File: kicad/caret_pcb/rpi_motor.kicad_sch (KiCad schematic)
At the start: 6 parts, among them J12 X+, J13 Y+, J14 Raspberry_Pi_2_3, J15 PWR IN

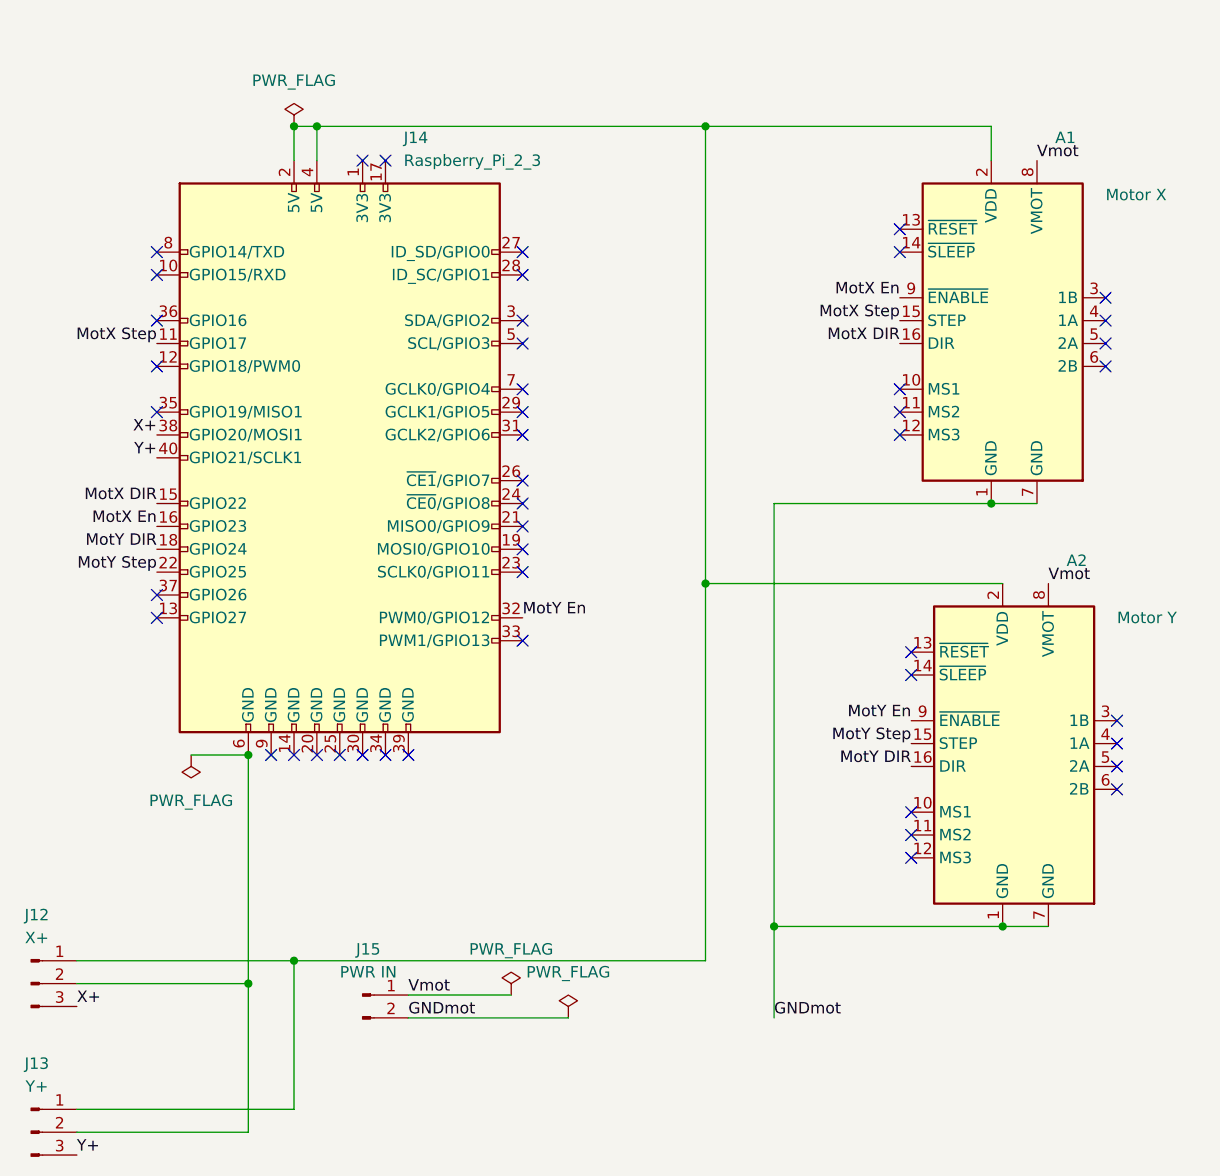
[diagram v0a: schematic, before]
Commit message: caret_pcb: fix piezo sensor power line, fix rpi shield schematic
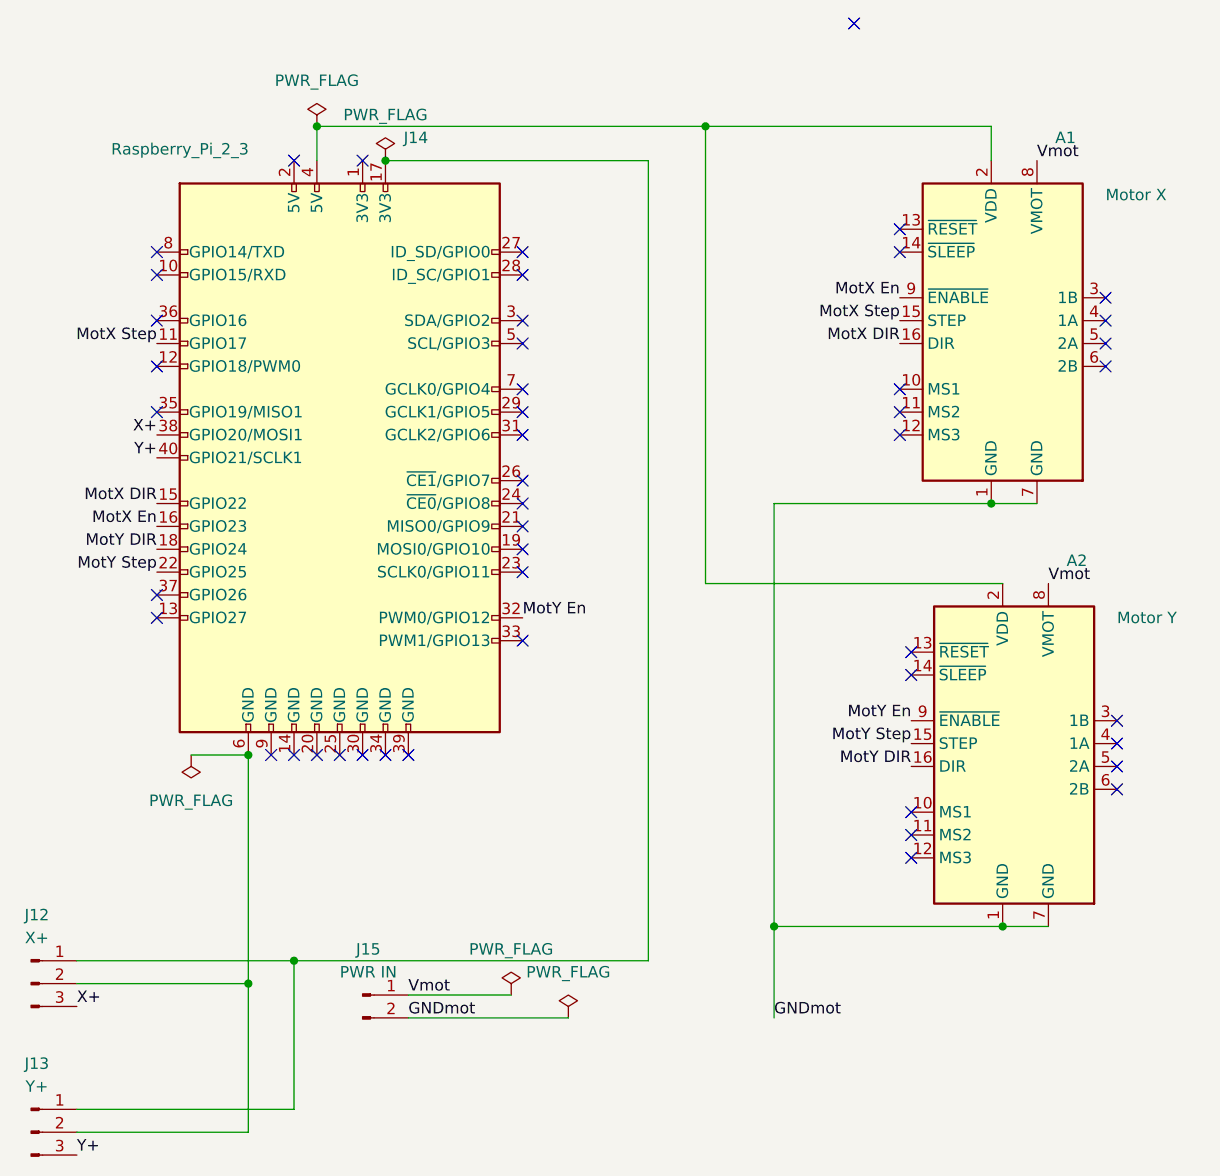
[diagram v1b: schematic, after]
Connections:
- net at A1.2 (VDD), A2.2 (VDD), J14.4 (5V): no longer J12.1 (Pin_1), J13.1 (Pin_1), J14.2 (5V)
- net at J14.17 (3V3): now also J12.1 (Pin_1), J13.1 (Pin_1)
- no-connect marks 47 -> 48
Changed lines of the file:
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@@
 (kicad_sch (version 20211123) (generator eeschema)
   (paper "A4")
-  (junction (at 135.89 87.63) (diameter 0) (color 0 0 0 0)
-  )
   (junction (at 168.91 125.73) (diameter 0) (color 0 0 0 0)
   )
@@
   (junction (at 85.09 106.68) (diameter 0) (color 0 0 0 0)
   )
-  (junction (at 90.17 36.83) (diameter 0) (color 0 0 0 0)
-  )
   (junction (at 92.71 36.83) (diameter 0) (color 0 0 0 0)
   )
   (junction (at 143.51 125.73) (diameter 0) (color 0 0 0 0)
+  )
+  (junction (at 100.33 40.64) (diameter 0) (color 0 0 0 0)
   )
   (junction (at 167.64 78.74) (diameter 0) (color 0 0 0 0)
@@
   (no_connect (at 158.75 118.11))
   (no_connect (at 157.48 50.8))
+  (no_connect (at 152.4 25.4))
+  (no_connect (at 97.79 40.64))
+  (no_connect (at 90.17 40.64))
   (no_connect (at 158.75 115.57))
   (no_connect (at 158.75 95.25))
@@
   (no_connect (at 115.57 83.82))
   (no_connect (at 115.57 81.28))
-  (no_connect (at 100.33 40.64))
-  (no_connect (at 97.79 40.64))
   (no_connect (at 74.93 50.8))
   (no_connect (at 74.93 53.34))
@@
     (stroke (width 0) (type default) (color 0 0 0 0))
   )
-  (wire (pts (xy 90.17 36.83) (xy 92.71 36.83))
-    (stroke (width 0) (type default) (color 0 0 0 0))
-  )
-  (wire (pts (xy 90.17 40.64) (xy 90.17 36.83))
-    (stroke (width 0) (type default) (color 0 0 0 0))
-  )
   (wire (pts (xy 168.91 87.63) (xy 135.89 87.63))
     (stroke (width 0) (type default) (color 0 0 0 0))
@@
     (stroke (width 0) (type default) (color 0 0 0 0))
   )
+  (wire (pts (xy 100.33 40.64) (xy 129.54 40.64))
+    (stroke (width 0) (type default) (color 0 0 0 0))
+  )
   (wire (pts (xy 78.74 106.68) (xy 85.09 106.68))
     (stroke (width 0) (type default) (color 0 0 0 0))
@@
     (stroke (width 0) (type default) (color 0 0 0 0))
   )
-  (wire (pts (xy 90.17 129.54) (xy 135.89 129.54))
+  (wire (pts (xy 90.17 129.54) (xy 129.54 129.54))
+    (stroke (width 0) (type default) (color 0 0 0 0))
+  )
+  (wire (pts (xy 129.54 40.64) (xy 129.54 129.54))
     (stroke (width 0) (type default) (color 0 0 0 0))
   )
@@
   )
   (wire (pts (xy 135.89 36.83) (xy 167.64 36.83))
-    (stroke (width 0) (type default) (color 0 0 0 0))
-  )
-  (wire (pts (xy 135.89 129.54) (xy 135.89 87.63))
     (stroke (width 0) (type default) (color 0 0 0 0))
   )
@@
     (pin "2")
   )
-  (symbol (lib_id "power:PWR_FLAG") (at 90.17 36.83 0) (unit 1)
-    (in_bom yes) (on_board yes) (fields_autoplaced)
-    (property "Reference" "#FLG01" (id 0) (at 90.17 34.925 0)
-      (effects (font (size 1.27 1.27)) hide)
-    )
-    (property "Value" "PWR_FLAG" (id 1) (at 90.17 31.75 0))
-    (property "Footprint" "" (id 2) (at 90.17 36.83 0)
-      (effects (font (size 1.27 1.27)) hide)
-    )
-    (property "Datasheet" "~" (id 3) (at 90.17 36.83 0)
+  (symbol (lib_id "power:PWR_FLAG") (at 92.71 36.83 0) (unit 1)
+    (in_bom yes) (on_board yes) (fields_autoplaced)
+    (property "Reference" "#FLG01" (id 0) (at 92.71 34.925 0)
+      (effects (font (size 1.27 1.27)) hide)
+    )
+    (property "Value" "PWR_FLAG" (id 1) (at 92.71 31.75 0))
+    (property "Footprint" "" (id 2) (at 92.71 36.83 0)
+      (effects (font (size 1.27 1.27)) hide)
+    )
+    (property "Datasheet" "~" (id 3) (at 92.71 36.83 0)
+      (effects (font (size 1.27 1.27)) hide)
+    )
+    (pin "1")
+  )
+  (symbol (lib_id "power:PWR_FLAG") (at 100.33 40.64 0) (unit 1)
+    (in_bom yes) (on_board yes) (fields_autoplaced)
+    (property "Reference" "#FLG0106" (id 0) (at 100.33 38.735 0)
+      (effects (font (size 1.27 1.27)) hide)
+    )
+    (property "Value" "PWR_FLAG" (id 1) (at 100.33 35.56 0))
+    (property "Footprint" "" (id 2) (at 100.33 40.64 0)
+      (effects (font (size 1.27 1.27)) hide)
+    )
+    (property "Datasheet" "~" (id 3) (at 100.33 40.64 0)
       (effects (font (size 1.27 1.27)) hide)
     )
@@
   )
   (symbol (lib_id "Connector:Raspberry_Pi_2_3") (at 95.25 73.66 0) (unit 1)
-    (in_bom yes) (on_board yes) (fields_autoplaced)
+    (in_bom yes) (on_board yes)
     (property "Reference" "J14" (id 0) (at 102.3494 38.1 0)
       (effects (font (size 1.27 1.27)) (justify left))
     )
-    (property "Value" "Raspberry_Pi_2_3" (id 1) (at 102.3494 40.64 0)
-      (effects (font (size 1.27 1.27)) (justify left))
-    )
+    (property "Value" "Raspberry_Pi_2_3" (id 1) (at 69.85 39.37 0)
+      (effects (font (size 1.27 1.27)) (justify left))
+    )
